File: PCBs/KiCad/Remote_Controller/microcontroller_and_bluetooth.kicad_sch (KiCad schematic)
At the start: 0 parts

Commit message: Added ESP32-C3-MINI-1 to remote controller
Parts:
- added C? (x2): 0.1uF, symbol Device:C
- added C? (x2): 22uF, symbol Device:C
- added R?: R, symbol Device:R
- added SW?: SW_Push, symbol Switch:SW_Push
- added U?: ESP32-C3-MINI-1, ESP32-MINI-1-N4:XCVR_ESP32-MINI-1-N4, symbol ESP32-C3-MINI-1:ESP32-C3-MINI-1
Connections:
- new net: C?.1, C?.1, R?.2, SW?.2, U?.8 (EN)
- new net +3.3V: C?.1, C?.1, R?.1, U?.3 (3V3)
- new net GND: C?.2, C?.2, C?.2, C?.2, SW?.1, U?.1 (GND), U?.2 (GND), U?.27 (GND), U?.38 (GND), U?.39 (GND), U?.40 (GND), U?.41 (GND), U?.42 (GND), U?.43 (GND), U?.44 (GND), U?.45 (GND), U?.46 (GND), U?.47 (GND), U?.48 (GND), U?.49 (GND), U?.50 (GND), U?.51 (GND), U?.52 (GND), U?.53 (GND), U?.54 (GND), U?.55 (GND)

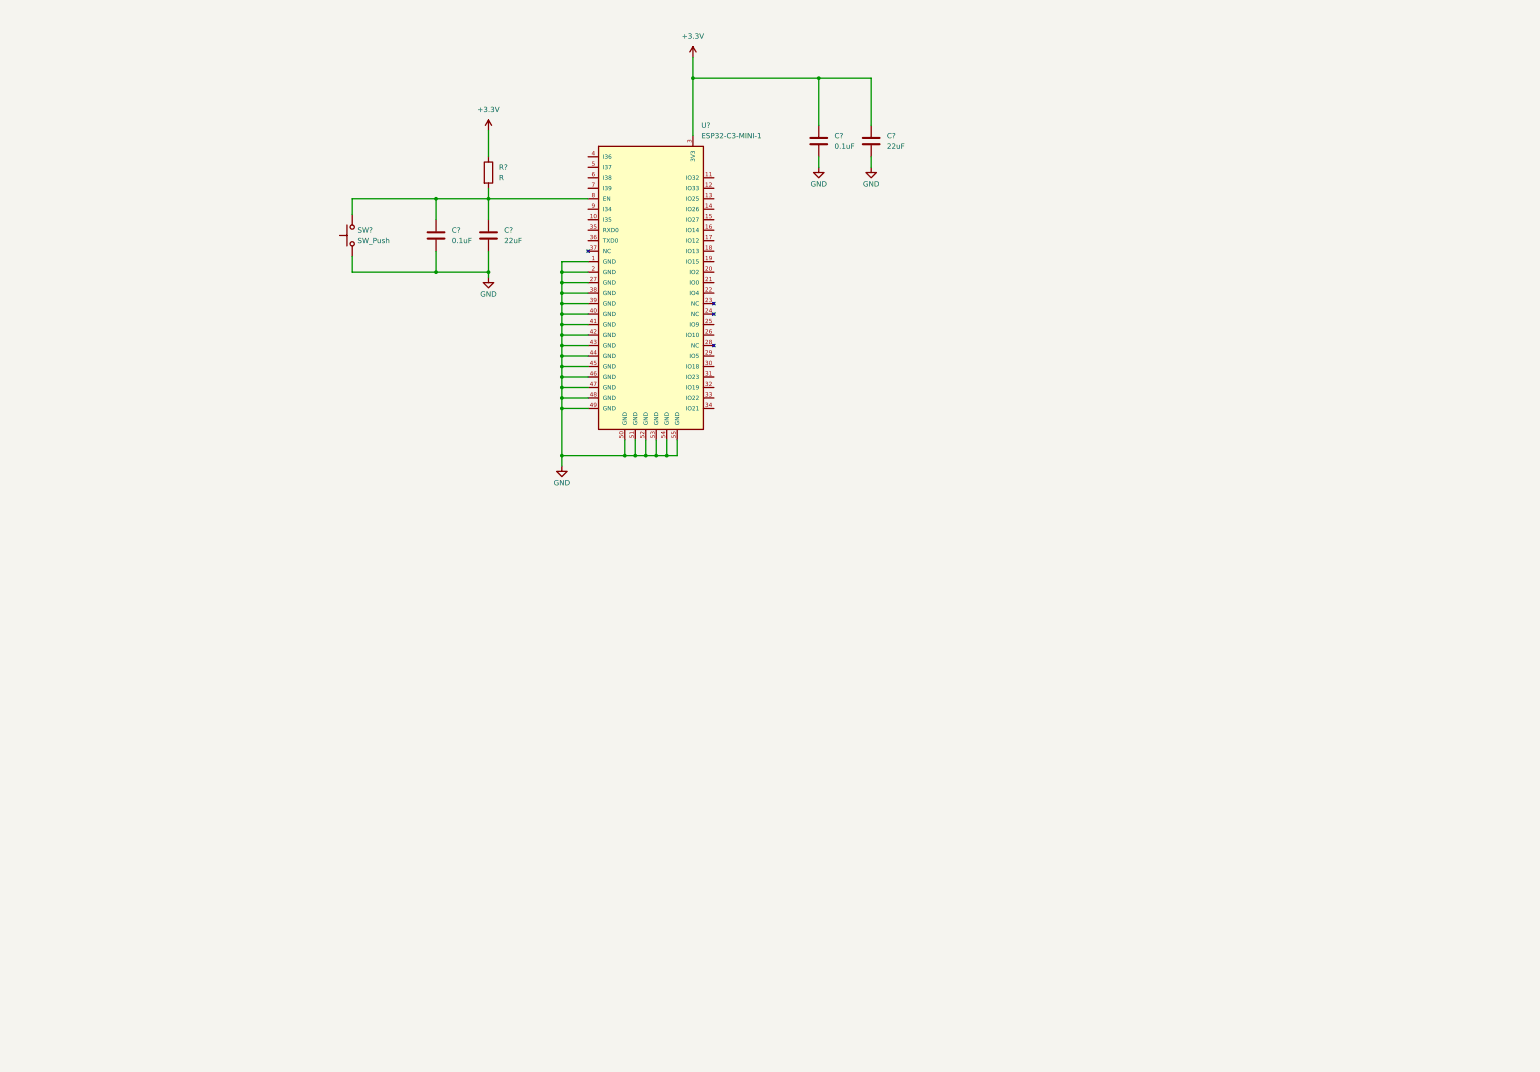
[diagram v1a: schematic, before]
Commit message: Add USB_C connector and USB_UART programmer to remote controller
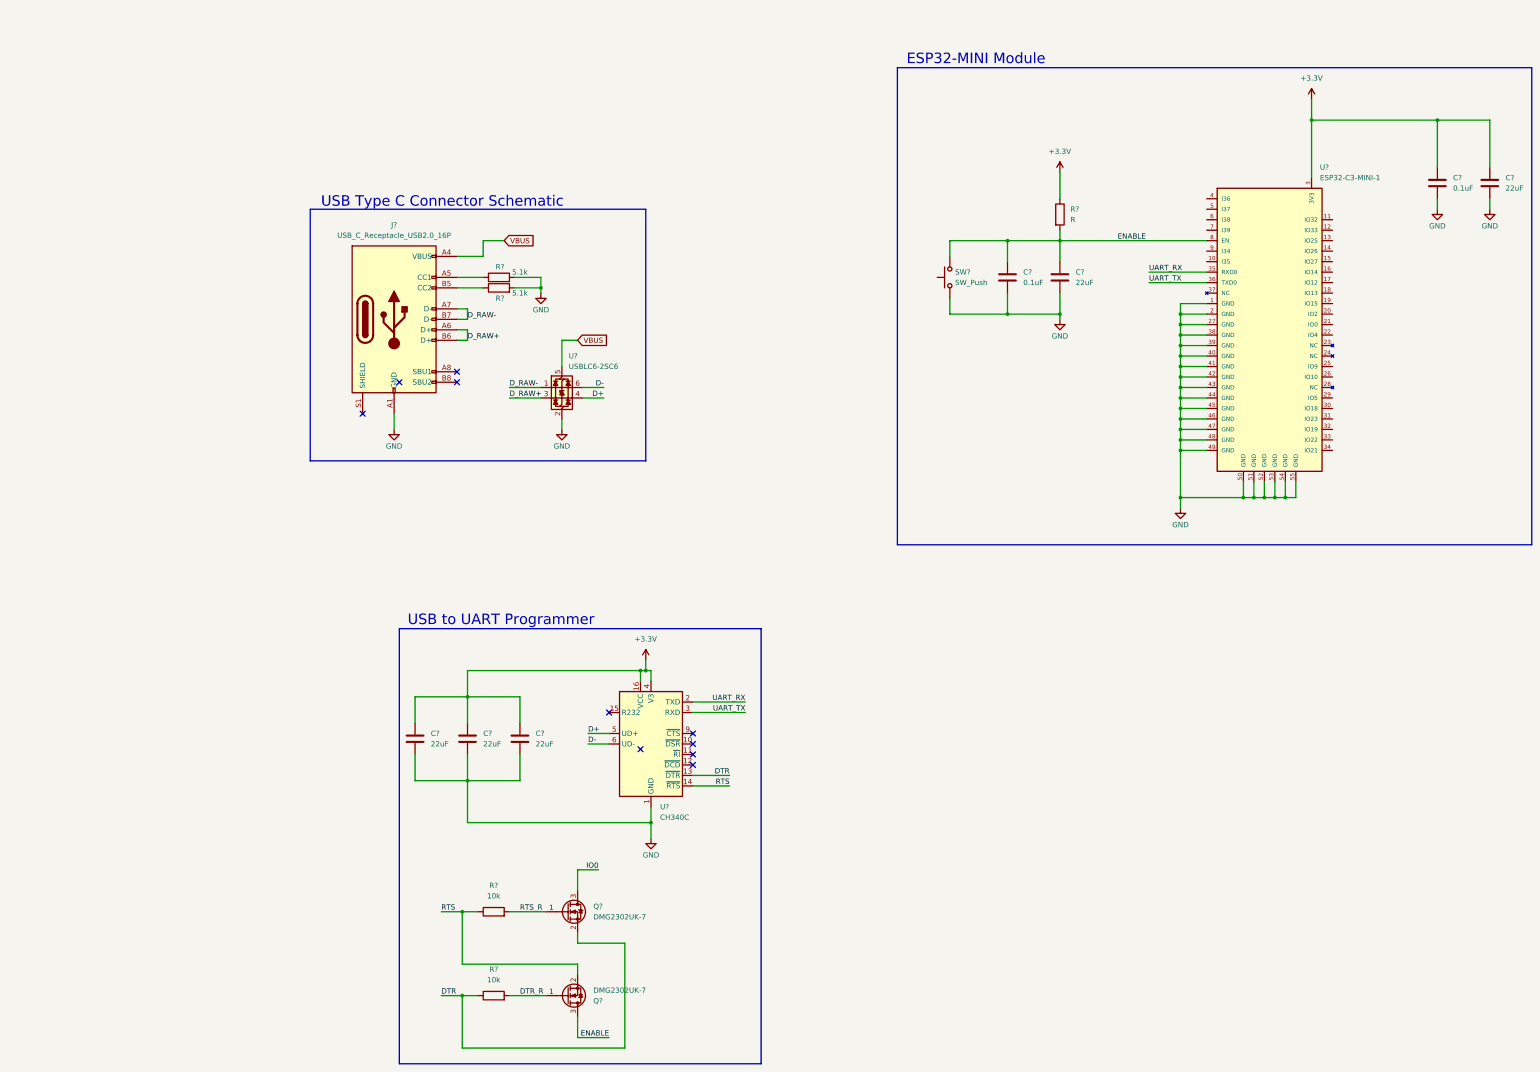
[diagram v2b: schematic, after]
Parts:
- added C? (x3): 22uF, symbol Device:C
- added J?: USB_C_Receptacle_USB2.0_16P, symbol Connector:USB_C_Receptacle_USB2.0_16P
- added Q? (x2): DMG2302UK-7, Package_TO_SOT_SMD:SOT-23, symbol Transistor_FET:DMG2302U
- added R? (x2): 5.1k, symbol Device:R
- added R? (x2): 10k, symbol Device:R
- added U?: USBLC6-2SC6, Package_TO_SOT_SMD:SOT-23-6, symbol Power_Protection:USBLC6-2SC6
- added U?: CH340C, Package_SO:SOIC-16_3.9x9.9mm_P1.27mm, symbol Interface_USB:CH340C
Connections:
- net +3.3V: now also C?.1, C?.1, C?.1, U?.16 (VCC), U?.4 (V3)
- net GND: now also C?.2, C?.2, C?.2, J?.A1 (GND), J?.A12 (GND), J?.B1 (GND), J?.B12 (GND), R?.2, R?.2, U?.1 (GND), U?.2 (GND)
- net ENABLE: now reaches C?.1, C?.1, R?.2, SW?.2, U?.8 (EN)
- net ENABLE: now also Q?.3 (D)
- net UART_RX: now reaches U?.35 (RXD0)
- net UART_RX: now also U?.2 (TXD)
- net UART_TX: now reaches U?.36 (TXD0)
- net UART_TX: now also U?.3 (RXD)
- new net: J?.A5 (CC1), R?.1
- new net: J?.B5 (CC2), R?.1
- new net D+: U?.4 (I/O2), U?.5 (UD+)
- new net D-: U?.6 (I/O1), U?.6 (UD-)
- new net DTR: Q?.2 (S), R?.1, U?.13 (~{DTR})
- new net DTR_R: Q?.1 (G), R?.2
- new net D_RAW+: J?.A6 (D+), J?.B6 (D+), U?.3 (I/O2)
- new net D_RAW-: J?.A7 (D-), J?.B7 (D-), U?.1 (I/O1)
- new net IO0: Q?.3 (D)
- new net RTS: Q?.2 (S), R?.1, U?.14 (~{RTS})
- new net RTS_R: Q?.1 (G), R?.2
- new net VBUS: J?.A4 (VBUS), J?.A9 (VBUS), J?.B4 (VBUS), J?.B9 (VBUS), U?.5 (VBUS)
- no-connect marks 0 -> 10
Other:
- note added: "ESP32-MINI Module"
- note added: "USB Type C Connector Schematic"
- note added: "USB to UART Programmer"
- moved on the sheet: C?, R?, SW?, U?

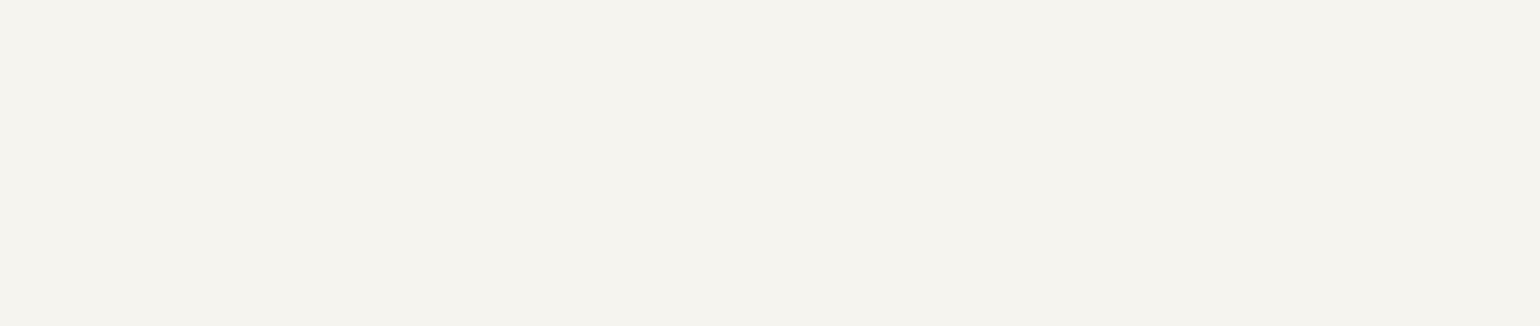
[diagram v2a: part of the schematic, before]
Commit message: Numbered all of the schematics
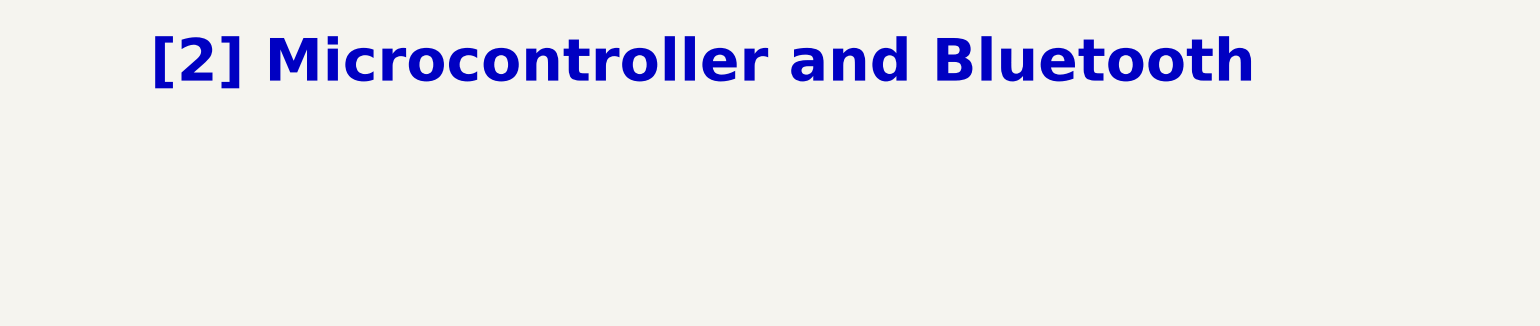
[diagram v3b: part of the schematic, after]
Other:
- note added: "[2] Microcontroller and Bluetooth"
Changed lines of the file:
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@@
+		)
+	)
+	(text "[2] Microcontroller and Bluetooth"
+		(exclude_from_sim no)
+		(at 82.296 22.86 0)
+		(effects
+			(font
+				(size 5.08 5.08)
+				(thickness 1.016)
+				(bold yes)
+			)
 		)
 	)

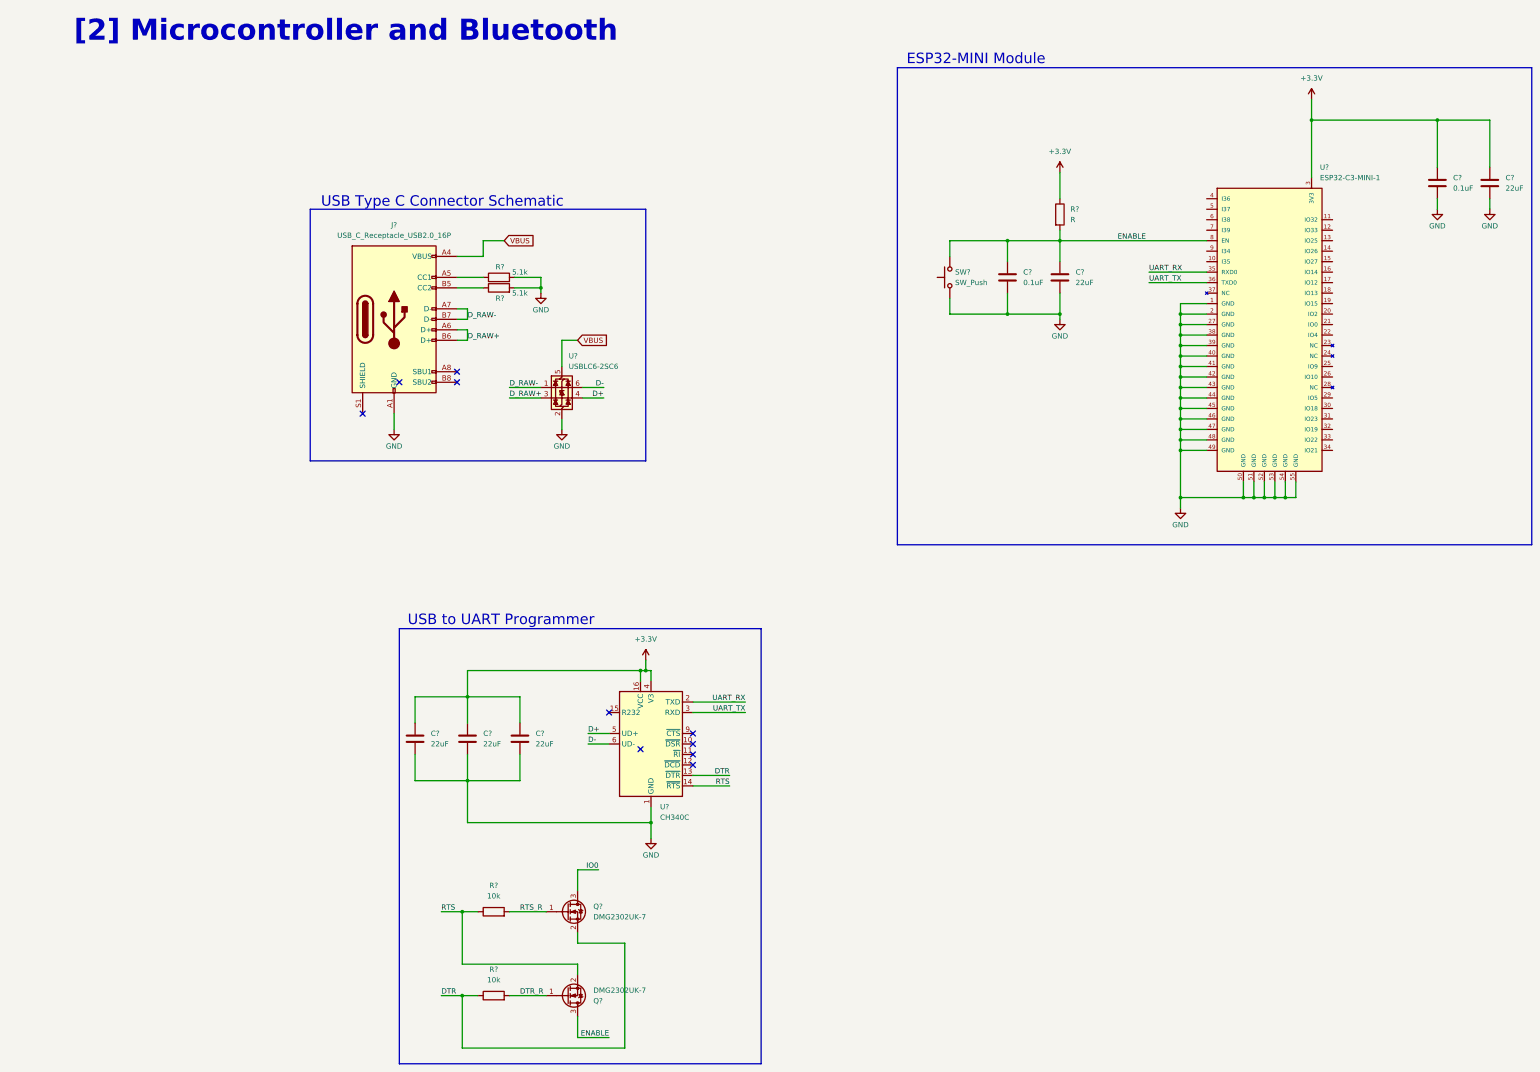
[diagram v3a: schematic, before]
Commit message: Decided on microcontroller ESP32-WROOM-32E(-N4)
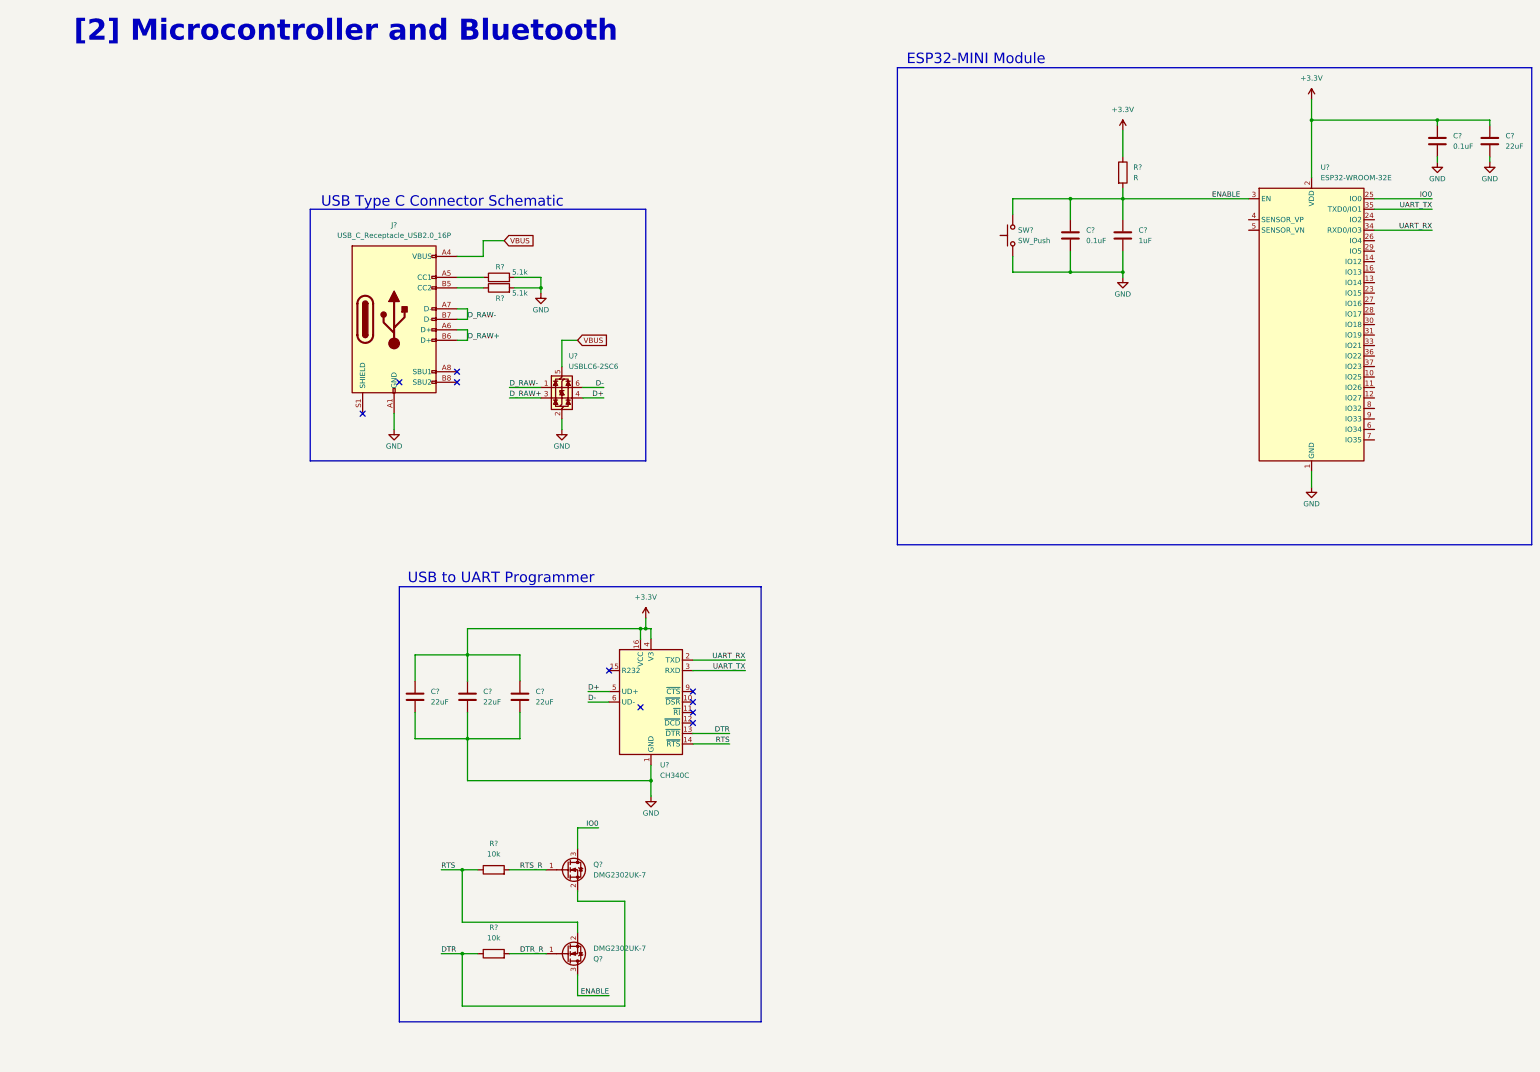
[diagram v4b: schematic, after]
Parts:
- removed U?: ESP32-C3-MINI-1, ESP32-MINI-1-N4:XCVR_ESP32-MINI-1-N4, symbol ESP32-C3-MINI-1:ESP32-C3-MINI-1
- added U?: ESP32-WROOM-32E, RF_Module:ESP32-WROOM-32D, symbol RF_Module:ESP32-WROOM-32E
- C?: value 22uF -> 1uF
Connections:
- net +3.3V: now also U?.2 (VDD)
- net ENABLE: now also U?.3 (EN)
- net GND: now also U?.1 (GND), U?.15 (GND), U?.38 (GND), U?.39 (GND)
- net IO0: now also U?.25 (IO0)
- net UART_RX: now also U?.34 (RXD0/IO3)
- net UART_TX: now also U?.35 (TXD0/IO1)
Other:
- moved on the sheet: C?, Q?, R?, SW?, U?

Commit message: Update programming circuit for remote controller
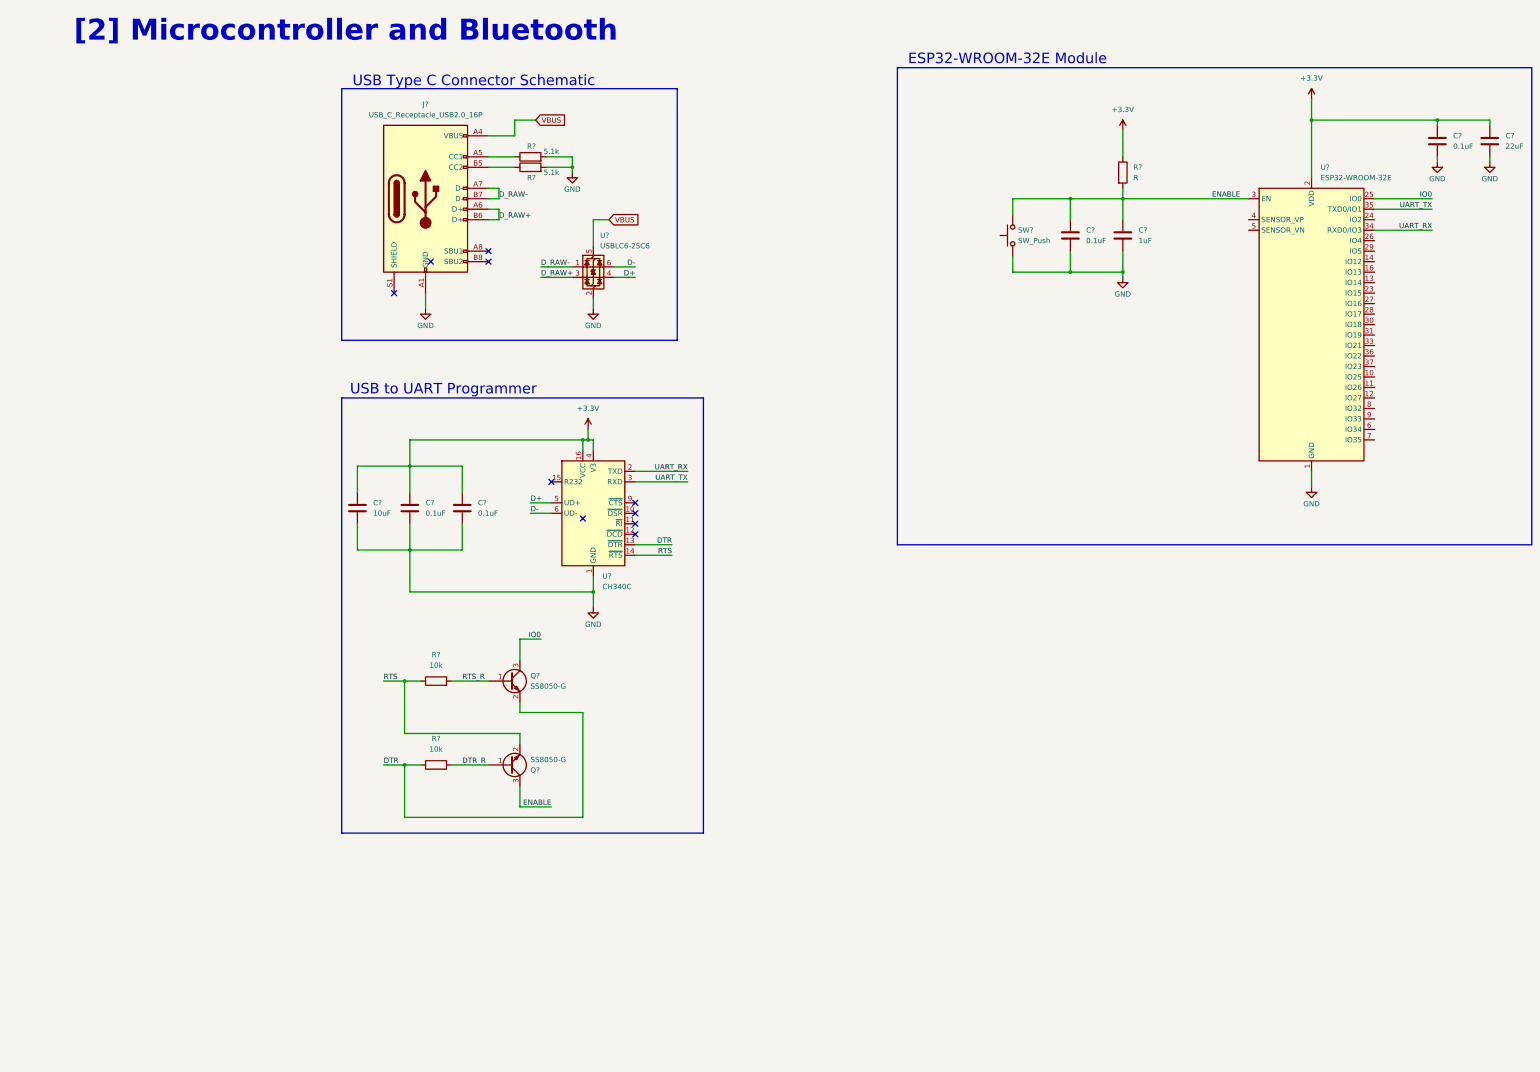
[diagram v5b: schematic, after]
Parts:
- removed Q? (x2): DMG2302UK-7, Package_TO_SOT_SMD:SOT-23, symbol Transistor_FET:DMG2302U
- added Q? (x2): SS8050-G, Package_TO_SOT_SMD:SOT-23, symbol Device:Q_NPN_BEC
- C?: value 22uF -> 10uF
- C? (x2): value 22uF -> 0.1uF
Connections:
- net DTR: now also Q?.2 (E)
- net DTR_R: now also Q?.1 (B)
- net ENABLE: now also Q?.3 (C)
- net IO0: now also Q?.3 (C)
- net RTS: now also Q?.2 (E)
- net RTS_R: now also Q?.1 (B)
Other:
- note added: "ESP32-WROOM-32E Module"
- note removed: "ESP32-MINI Module"
- moved on the sheet: C?, J?, R?, U?
